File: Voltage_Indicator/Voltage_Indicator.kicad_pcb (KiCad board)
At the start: 2 copper layers, 68.7 x 60.4 mm, 24 parts, among them J1 PET-02-XX-X-VT-LC, K1 VORA1150-X017T, U1 LM393LVQDDFRQ1, U2 IPBT-102-H1-XX-S-RA

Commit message: Voltage Indicator All Files
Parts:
- J1: footprint Footprints:SAMTEC_PET-02-XX-X-VT-LC -> Footprints:SAMTEC_PES-02-01-X-RA-SD
- R1, R3, R4: footprint Resistor_SMD:R_0201_0603Metric -> SDM_MiscFootprint:R_1206_3216Metric
- R5: footprint Resistor_SMD:R_0201_0603Metric -> Resistor_SMD:R_1206_3216Metric
- moved J1 1.83 mm to (148.0, 102.4), turned to -90 degrees
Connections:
- R1 pad 1: 01 -> /HV+
- R6 pad 2: 02 -> /HV-
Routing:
- net 02: track 36.9 -> 0.00 mm
- net /HV-: track 0.00 -> 32.5 mm
- net 01: track 32.2 -> 0.00 mm
- net /HV+: track 0.00 -> 29.0 mm
- net /12V Master: track 35.0 -> 34.0 mm
- net /V_DIV: track 35.7 -> 34.7 mm
- net Net-(R1-Pad2): track 8.17 -> 7.64 mm
- added copper zone on F.Cu, net GND
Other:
- board size 68.7 x 60.4 mm -> 71 x 60.4 mm

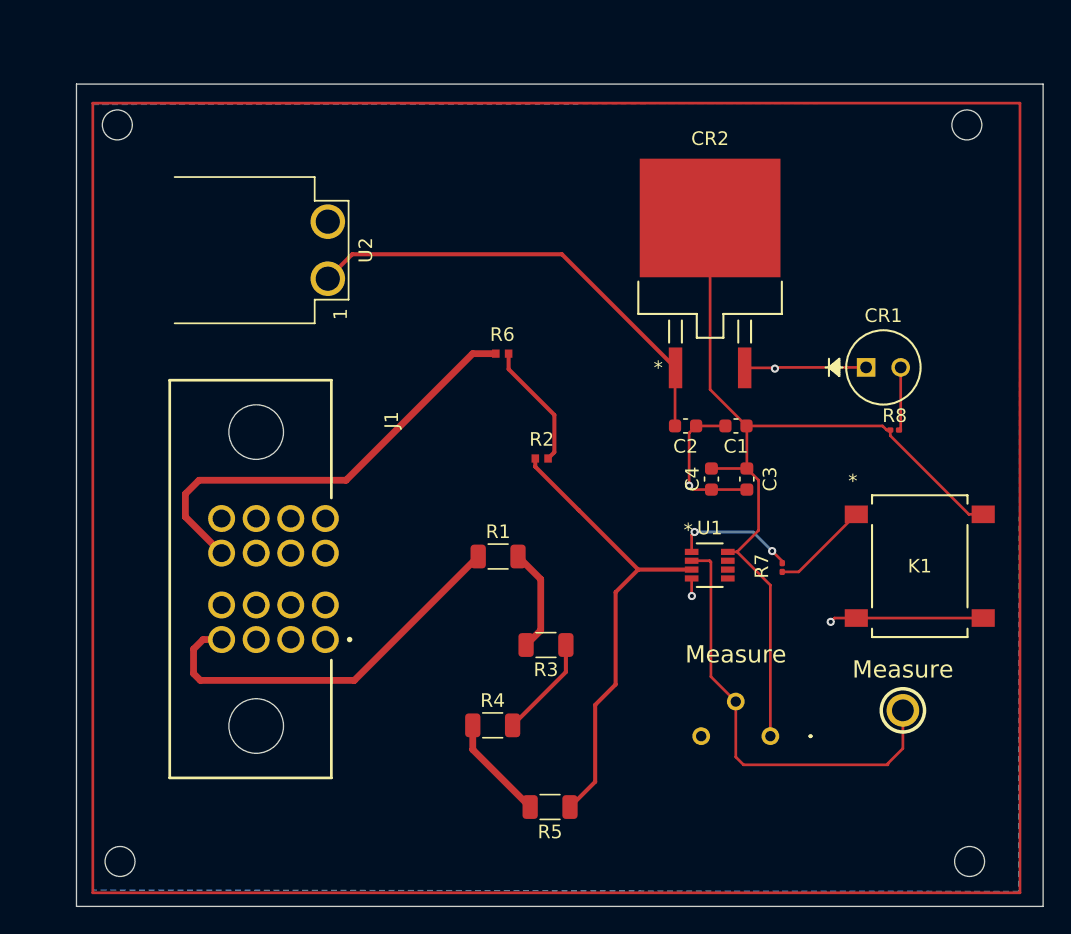
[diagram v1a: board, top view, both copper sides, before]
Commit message: BSPD V1.2, Shutdown Circuit, Charging Shutdown Circuit, Voltage Indicator
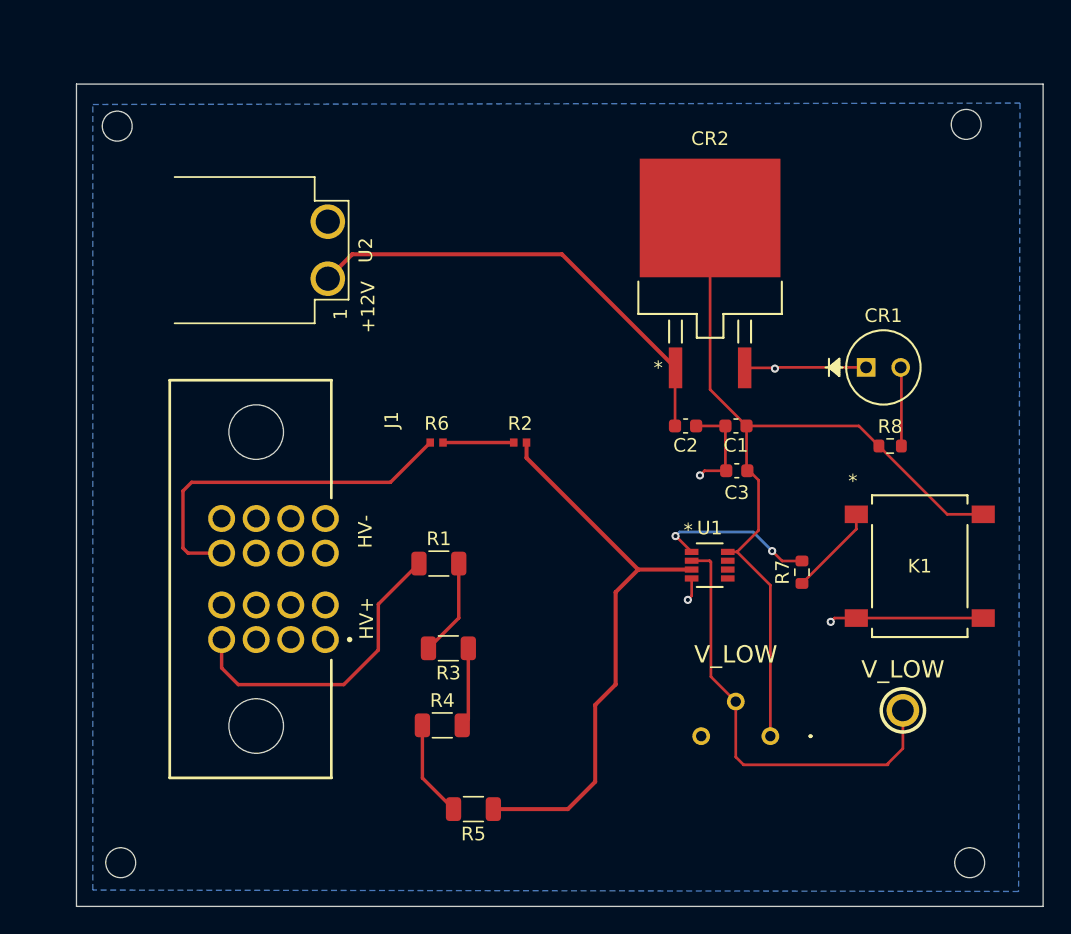
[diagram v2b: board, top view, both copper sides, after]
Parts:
- removed C4: 1uF, Capacitor_SMD:C_0603_1608Metric
- removed the REF** at (200.4, 123.1)
- removed the REF** at (138.0, 123.1)
- removed the REF** at (200.2, 69.0)
- removed the REF** at (137.8, 69.0)
- added REF**: MountingHole_2.2mm_M2, MountingHole:MountingHole_2.2mm_M2, F.Cu at (200.2, 69.0)
- added REF**: MountingHole_2.2mm_M2, MountingHole:MountingHole_2.2mm_M2, F.Cu at (138.0, 123.2)
- added REF**: MountingHole_2.2mm_M2, MountingHole:MountingHole_2.2mm_M2, F.Cu at (200.4, 123.2)
- added REF**: MountingHole_2.2mm_M2, MountingHole:MountingHole_2.2mm_M2, F.Cu at (137.8, 69.1)
- R7, R8: footprint Resistor_SMD:R_0201_0603Metric -> Resistor_SMD:R_0603_1608Metric
- moved R6 8.11 mm to (161.3, 92.3)
- moved R3 7.17 mm to (162.1, 107.4)
- moved R5 5.63 mm to (164.0, 119.3)
- moved R1 4.38 mm to (161.4, 101.2)
- moved R4 3.70 mm to (161.7, 113.1)
- moved R2 1.97 mm to (167.4, 92.3), turned to 180 degrees
- moved R7 1.49 mm to (188.1, 101.9)
- moved R8 1.22 mm to (194.6, 92.6)
- moved C3 0.96 mm to (183.3, 94.4), turned to 0 degrees
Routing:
- net /V_DIV: track 34.7 -> 41.9 mm
- net /HV+: track 29.0 -> 22.7 mm
- net /HV-: track 32.5 -> 26.8 mm
- net Net-(R2-Pad2): track 9.28 -> 5.19 mm
- net GND: track 32.8 -> 29.6 mm
- net /V_IND: track 9.03 -> 12.0 mm
- net +5V: track 64.8 -> 62.1 mm
- net Net-(R3-Pad1): track 7.52 -> 5.84 mm
- net Net-(CR1-Pad2): track 4.65 -> 5.79 mm
- net Net-(R4-Pad1): track 7.75 -> 7.10 mm
- removed copper zone on F.Cu, net GND
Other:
- board text added: "+12V"
- board text added: "HV+"
- board text added: "HV-"

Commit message: BSPD, Shutdown/Charging Shutdown, & Voltage Indicator final changes
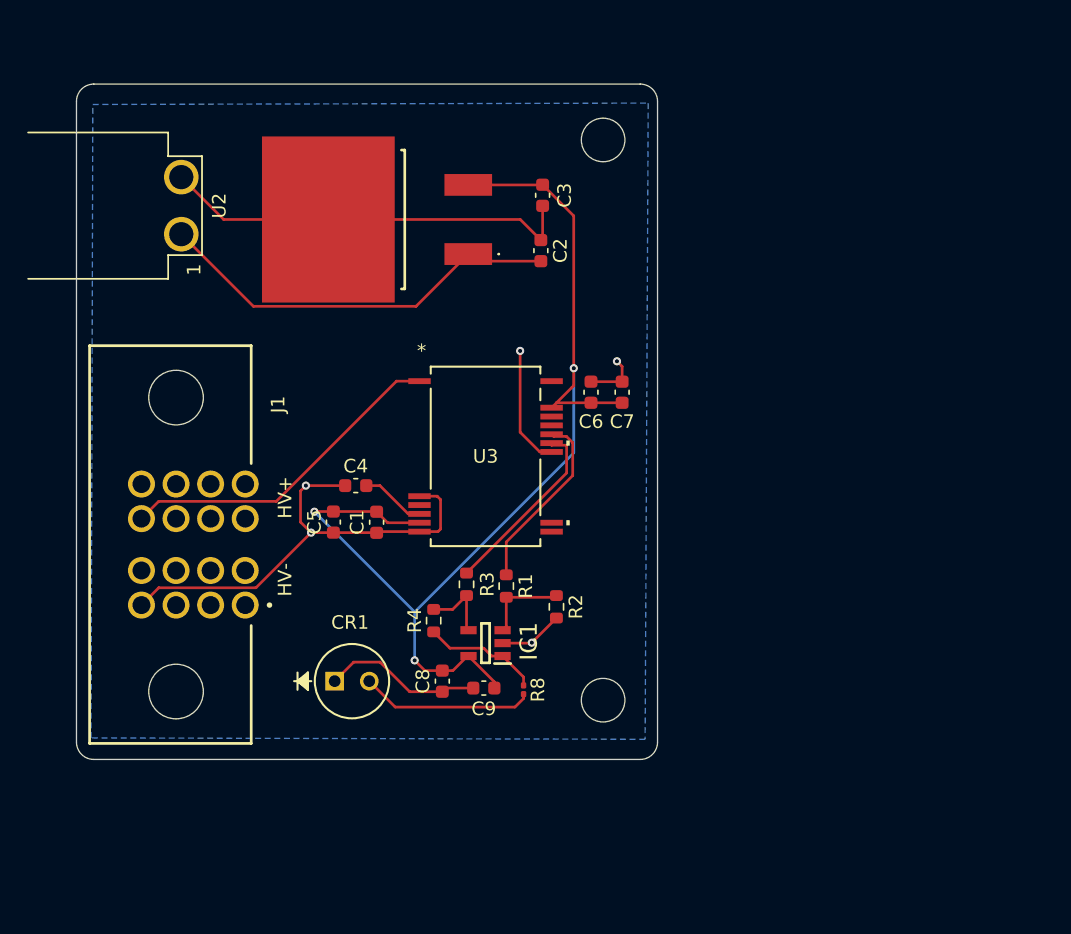
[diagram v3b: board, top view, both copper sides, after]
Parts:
- removed K1: VORA1150-X017T, Footprints:SOP_VORA1150-X017T_VIS
- removed R5: 500K, Resistor_SMD:R_1206_3216Metric
- removed R6: 8.4K, Footprints:RES_ERA2A_PAN
- removed R7: 1.2K, Resistor_SMD:R_0603_1608Metric
- removed RED_TP1: 5005, Footprints:5005
- removed the REF** at (200.2, 69.0)
- removed the REF** at (138.0, 123.2)
- removed the REF** at (200.4, 123.2)
- removed the REF** at (137.8, 69.1)
- removed U1: LM393LVQDDFRQ1, Footprints:SOT-23-THIN8_DDF_TEX
- removed VR1: 10k, Footprints:3386P1103TLF
- added C4: 100pF, Capacitor_SMD:C_0603_1608Metric, F.Cu at (155.3, 95.5)
- added C5: 1uF, Capacitor_SMD:C_0603_1608Metric, F.Cu at (153.7, 98.2)
- added C6: 1uF, Capacitor_SMD:C_0603_1608Metric, F.Cu at (172.6, 88.6)
- added C7: 100nF, Capacitor_SMD:C_0603_1608Metric, F.Cu at (174.9, 88.6)
- added C8: 100nF, Capacitor_SMD:C_0603_1608Metric, F.Cu at (161.7, 109.9)
- added C9: 1uF, Capacitor_SMD:C_0603_1608Metric, F.Cu at (164.7, 110.4)
- added IC1: TLV2371QDBVRQ1, Footprints:SOT95P280X145-5N, F.Cu at (164.8, 107.1)
- added REF**: MountingHole_3.2mm_M3, MountingHole:MountingHole_3.2mm_M3, F.Cu at (173.5, 111.3)
- added REF**: MountingHole_3.2mm_M3, MountingHole:MountingHole_3.2mm_M3, F.Cu at (173.5, 70.1)
- added U3: PAMC0381D10QDFXRQ1, Footprints:SSOP15_DFX_TEX, F.Cu at (164.8, 93.3)
- C1: value 1uF -> 100nF
- CR2: footprint Footprints:D2PAK_STM -> Footprints:L7805ACD2TTR
- R1, R3, R4: value 500K -> 10k; footprint SDM_MiscFootprint:R_1206_3216Metric -> Resistor_SMD:R_0603_1608Metric
- R2: value 8.4K -> 10k; footprint Footprints:RES_ERA2A_PAN -> Resistor_SMD:R_0603_1608Metric
- R8: footprint Resistor_SMD:R_0603_1608Metric -> Resistor_SMD:R_0201_0603Metric
- moved CR1 45.3 mm to (153.8, 109.9)
- moved R8 32.3 mm to (167.6, 110.5), turned to -90 degrees
- moved C1 27.3 mm to (156.8, 98.2), turned to 90 degrees
- moved CR2 24.8 mm to (156.7, 75.9), turned to 90 degrees
- moved C3 24.8 mm to (169.0, 74.2), turned to 90 degrees
- moved C2 16.7 mm to (168.9, 78.2), turned to -90 degrees
- moved R2 12.4 mm to (170.1, 104.4), turned to -90 degrees
- moved U2 11.2 mm to (130.7, 74.9)
- moved R4 7.72 mm to (161.0, 105.4), turned to -90 degrees
- moved J1 6.41 mm to (142.1, 99.8)
- moved R1 5.22 mm to (166.4, 102.9), turned to -90 degrees
- moved R3 4.88 mm to (163.4, 102.7), turned to 90 degrees
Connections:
- C1 pad 1: +5V -> /HV-
- C1 pad 2: GND -> +5V
- J1 pad P01_1: /HV+ -> /HV-
- J1 pad P02_1: /HV- -> /HV+
- R1 pad 1: /HV+ -> /OUT_P
- R1 pad 2: Net-(R1-Pad2) -> Net-(IC1-IN+)
- R2 pad 1: /V_DIV -> Net-(IC1-IN+)
- R2 pad 2: Net-(R2-Pad2) -> GND
- R3 pad 1: Net-(R3-Pad1) -> Net-(IC1-IN-)
- R3 pad 2: Net-(R1-Pad2) -> /OUT_N
- R4 pad 1: Net-(R4-Pad1) -> Net-(IC1-IN-)
- R4 pad 2: Net-(R3-Pad1) -> Net-(IC1-OUT)
- R8 pad 1: +5V -> Net-(IC1-OUT)
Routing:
- net /V_DIV: track 41.9 -> 0.00 mm
- net /V_LOW_REF: track 32.4 -> 0.00 mm
- net GND: track 29.6 -> 60.2 mm, vias 4 -> 3
- net +5V: track 62.1 -> 80.9 mm, vias 0 -> 3
- net /OUT_N: track 0.00 -> 13.7 mm
- net /OUT_P: track 0.00 -> 13.5 mm
- net /V_IND: track 12.0 -> 0.00 mm, vias 2 -> 0
- net Net-(IC1-OUT): track 0.00 -> 8.59 mm
- net /HV-: track 26.8 -> 34.9 mm, vias 0 -> 2
- net Net-(R1-Pad2): track 7.14 -> 0.00 mm
- net Net-(R4-Pad1): track 7.10 -> 0.00 mm
- net Net-(CR1-Pad2): track 5.79 -> 12.7 mm
- net Net-(K1-Pad1): track 6.73 -> 0.00 mm
- net Net-(IC1-IN+): track 0.00 -> 6.26 mm
- net Net-(R3-Pad1): track 5.84 -> 0.00 mm
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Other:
- board size 71 x 60.4 mm -> 42.7 x 49.6 mm
- board text removed: "+12V"

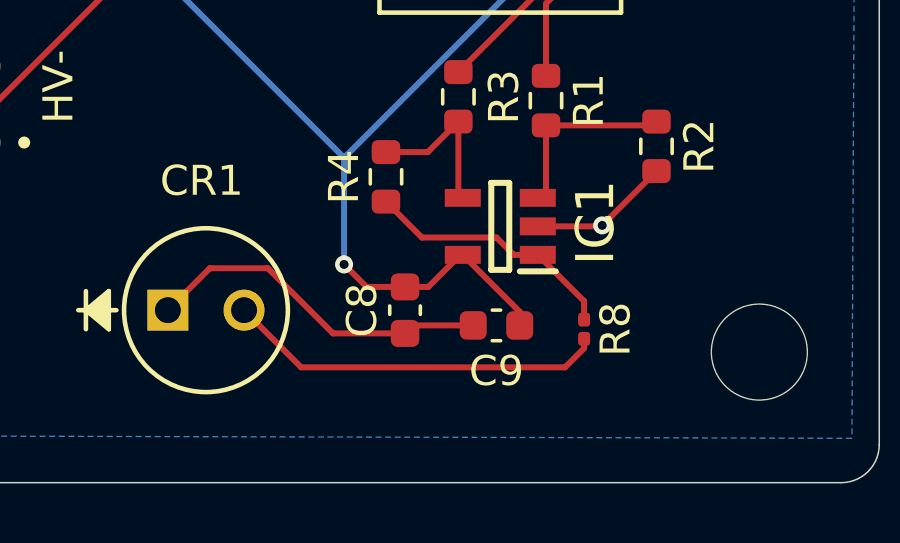
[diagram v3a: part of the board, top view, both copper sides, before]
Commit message: Voltage Indicator Fixed fr fr
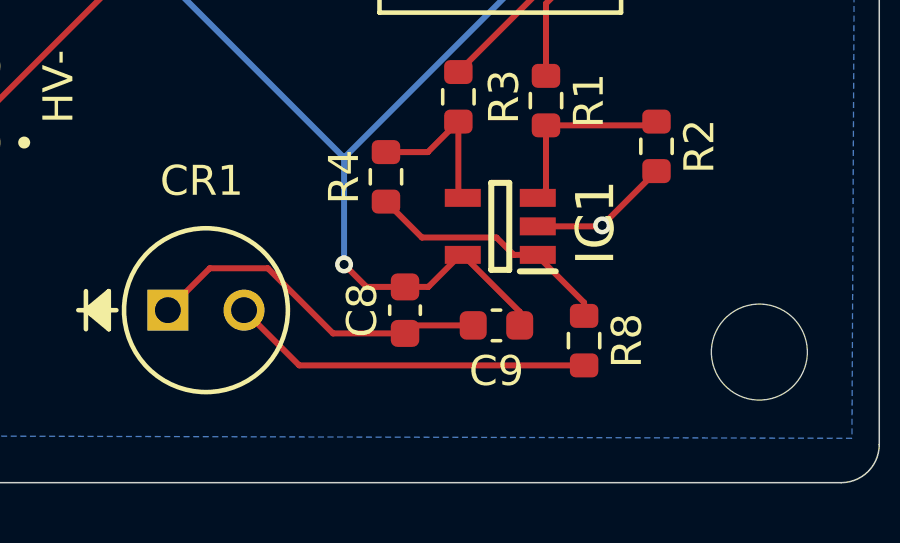
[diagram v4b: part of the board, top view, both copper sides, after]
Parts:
- R8: footprint Resistor_SMD:R_0201_0603Metric -> Resistor_SMD:R_0603_1608Metric
- moved R8 0.38 mm to (167.6, 110.9)
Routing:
- net Net-(CR1-Pad2): track 12.7 -> 12.1 mm
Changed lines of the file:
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@@
 		)
 	)
-	(footprint "Resistor_SMD:R_0201_0603Metric"
+	(footprint "Resistor_SMD:R_0603_1608Metric"
 		(layer "F.Cu")
-		(at 167.64 110.49 -90)
-		(descr "Resistor SMD 0201 (0603 Metric), square (rectangular) end terminal, IPC-7351 nominal, (Body size source: https://www.vishay.com/docs/20052/crcw0201e3.pdf), generated with kicad-footprint-generator")
+		(at 167.64 110.871 -90)
+		(descr "Resistor SMD 0603 (1608 Metric), square (rectangular) end terminal, IPC-7351 nominal, (Body size source: IPC-SM-782 page 72, https://www.pcb-3d.com/wordpress/wp-content/uploads/ipc-sm-782a_amendment_1_and_2.pdf), generated with kicad-footprint-generator")
 		(tags "resistor")
 		(property "Reference" "R8"
-			(at 0 -1.05 90)
+			(at 0 -1.43 270)
 			(layer "F.SilkS")
 			(effects
@@
 		)
 		(property "Value" "200"
-			(at 0 1.05 90)
+			(at 0 1.43 270)
 			(layer "F.Fab")
 			(effects
@@
 			)
 		)
-		(property "Datasheet" "~"
-			(at 0 0 90)
+		(property "Datasheet" ""
+			(at 0 0 270)
 			(layer "F.Fab")
 			(hide yes)
@@
 			)
 		)
-		(property "Description" "Resistor"
-			(at 0 0 90)
+		(property "Description" ""
+			(at 0 0 270)
 			(layer "F.Fab")
 			(hide yes)
@@
 		(sheetfile "Voltage_Indicator.kicad_sch")
 		(attr smd)
+		(fp_line
+			(start -0.237258 0.5225)
+			(end 0.237258 0.5225)
+			(stroke
+				(width 0.12)
+				(type solid)
+			)
+			(layer "F.SilkS")
+		)
+		(fp_line
+			(start -0.237258 -0.5225)
+			(end 0.237258 -0.5225)
+			(stroke
+				(width 0.12)
+				(type solid)
+			)
+			(layer "F.SilkS")
+		)
 		(fp_rect
-			(start -0.7 -0.35)
-			(end 0.7 0.35)
+			(start -1.48 -0.73)
+			(end 1.48 0.73)
 			(stroke
 				(width 0.05)
@@
 		)
 		(fp_rect
-			(start -0.3 -0.15)
-			(end 0.3 0.15)
+			(start -0.8 -0.4125)
+			(end 0.8 0.4125)
 			(stroke
 				(width 0.1)
@@
 		)
 		(fp_text user "${REFERENCE}"
-			(at 0 -0.68 90)
+			(at 0 0 270)
 			(layer "F.Fab")
 			(effects
 				(font
-					(size 0.25 0.25)
-					(thickness 0.04)
+					(size 0.4 0.4)
+					(thickness 0.06)
 				)
 			)
 		)
-		(pad "" smd roundrect
-			(at -0.345 0 270)
-			(size 0.318 0.36)
-			(layers "F.Paste")
-			(roundrect_rratio 0.25)
-		)
-		(pad "" smd roundrect
-			(at 0.345 0 270)
-			(size 0.318 0.36)
-			(layers "F.Paste")
-			(roundrect_rratio 0.25)
-		)
 		(pad "1" smd roundrect
-			(at -0.32 0 270)
-			(size 0.46 0.4)
-			(layers "F.Cu" "F.Mask")
+			(at -0.825 0 270)
+			(size 0.8 0.95)
+			(layers "F.Cu" "F.Mask" "F.Paste")
 			(roundrect_rratio 0.25)
 			(net 5 "Net-(IC1-OUT)")
@@
 		)
 		(pad "2" smd roundrect
-			(at 0.32 0 270)
-			(size 0.46 0.4)
-			(layers "F.Cu" "F.Mask")
+			(at 0.825 0 270)
+			(size 0.8 0.95)
+			(layers "F.Cu" "F.Mask" "F.Paste")
 			(roundrect_rratio 0.25)
 			(net 8 "Net-(CR1-Pad2)")
@@
 		)
 		(embedded_fonts no)
-		(model "${KICAD9_3DMODEL_DIR}/Resistor_SMD.3dshapes/R_0201_0603Metric.step"
+		(model "${KICAD9_3DMODEL_DIR}/Resistor_SMD.3dshapes/R_0603_1608Metric.step"
 			(offset
 				(xyz 0 0 0)
@@
 	)
 	(segment
-		(start 165.296 108.011)
-		(end 166.096 108.011)
+		(start 166.096 108.057)
+		(end 167.64 109.601)
 		(width 0.2)
 		(layer "F.Cu")
@@
 	)
 	(segment
-		(start 167.64 109.555)
+		(start 165.296 108.011)
 		(end 166.096 108.011)
 		(width 0.2)
@@
 	)
 	(segment
-		(start 167.64 110.17)
-		(end 167.64 109.555)
+		(start 167.64 109.601)
+		(end 167.64 110.046)
 		(width 0.2)
 		(layer "F.Cu")
@@
 	)
 	(segment
+		(start 166.096 108.011)
+		(end 166.096 108.057)
+		(width 0.2)
+		(layer "F.Cu")
+		(net 5)
+	)
+	(segment
 		(start 161.036 106.235)
 		(end 162.2342 107.4332)
@@
 	)
 	(segment
-		(start 167.64 111.125)
-		(end 167.64 110.81)
-		(width 0.2)
-		(layer "F.Cu")
-		(net 8)
-	)
-	(segment
-		(start 167.005 111.76)
-		(end 167.64 111.125)
-		(width 0.2)
-		(layer "F.Cu")
-		(net 8)
-	)
-	(segment
 		(start 156.30525 109.855)
-		(end 158.21025 111.76)
+		(end 158.14625 111.696)
 		(width 0.2)
 		(layer "F.Cu")
@@
 	)
 	(segment
-		(start 158.21025 111.76)
-		(end 167.005 111.76)
+		(start 158.14625 111.696)
+		(end 167.64 111.696)
 		(width 0.2)
 		(layer "F.Cu")
